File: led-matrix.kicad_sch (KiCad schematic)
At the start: 512 parts

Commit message: schematic updated
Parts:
- removed D129, D130, D131, D132, D133, D134, D135, D136, D137, D138, D139, D140, D141, D142, D143, D144, D145, D146, D147, D148, D149, D150, D151, D152, D153, D154, D155, D156, D157, D158, D159, D160, D161, D162, D163, D164, D165, D166, D167, D168, D169, D170, D171, D172, D173, D174, D175, D176, D177, D178, D179, D180, D181, D182, D183, D184, D185, D186, D187, D188, D189, D190, D191, D192, D193, D194, D195, D196, D197, D198, D199, D200, D201, D202, D203, D204, D205, D206, D207, D208, D209, D210, D211, D212, D213, D214, D215, D216, D217, D218, D219, D220, D221, D222, D223, D224, D225, D226, D227, D228, D229, D230, D231, D232, D233, D234, D235, D236, D237, D238, D239, D240, D241, D242, D243, D244, D245, D246, D247, D248, D249, D250, D251, D252, D253, D254, D255, D256, D257, D258, D259, D260, D261, D262, D263, D264, D265, D266, D267, D268, D269, D270, D271, D272, D273, D274, D275, D276, D277, D278, D279, D280, D281, D282, D283, D284, D285, D286, D287, D288, D289, D290, D291, D292, D293, D294, D295, D296, D297, D298, D299, D300, D301, D302, D303, D304, D305, D306, D307, D308, D309, D310, D311, D312, D313, D314, D315, D316, D317, D318, D319, D320, D321, D322, D323, D324, D325, D326, D327, D328, D329, D330, D331, D332, D333, D334, D335, D336, D337, D338, D339, D340, D341, D342, D343, D344, D345, D346, D347, D348, D349, D350, D351, D352, D353, D354, D355, D356, D357, D358, D359, D360, D361, D362, D363, D364, D365, D366, D367, D368, D369, D370, D371, D372, D373, D374, D375, D376, D377, D378, D379, D380, D381, D382, D383, D384, D385, D386, D387, D388, D389, D390, D391, D392, D393, D394, D395, D396, D397, D398, D399, D400, D401, D402, D403, D404, D405, D406, D407, D408, D409, D410, D411, D412, D413, D414, D415, D416, D417, D418, D419, D420, D421, D422, D423, D424, D425, D426, D427, D428, D429, D430, D431, D432, D433, D434, D435, D436, D437, D438, D439, D440, D441, D442, D443, D444, D445, D446, D447, D448, D449, D450, D451, D452, D453, D454, D455, D456, D457, D458, D459, D460, D461, D462, D463, D464, D465, D466, D467, D468, D469, D470, D471, D472, D473, D474, D475, D476, D477, D478, D479, D480, D481, D482, D483, D484, D485, D486, D487, D488, D489, D490, D491, D492, D493, D494, D495, D496, D497, D498, D499, D500, D501, D502, D503, D504, D505, D506, D507, D508, D509, D510, D511, D512: LED, PROJECT_FOOTPRINTS:LED_0805_2012Metric_45, symbol Device:LED
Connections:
- net at D118.1 (K), D22.1 (K), D54.1 (K)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: now also D102.1 (K), D38.1 (K), D6.1 (K), D70.1 (K)
- net at D81.2 (A), D82.2 (A), D83.2 (A)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: no longer D65.2 (A), D66.2 (A), D67.2 (A), D68.2 (A), D69.2 (A), D70.2 (A), D71.2 (A), D72.2 (A), D73.2 (A), D74.2 (A), D75.2 (A), D76.2 (A), D77.2 (A), D78.2 (A), D79.2 (A), D80.2 (A)
- net at D105.1 (K), D41.1 (K), D73.1 (K)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: now also D121.1 (K), D25.1 (K), D57.1 (K), D89.1 (K)
- net at D107.1 (K), D11.1 (K), D43.1 (K)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: now also D123.1 (K), D27.1 (K), D59.1 (K), D91.1 (K)
- net at D125.1 (K), D29.1 (K), D61.1 (K)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: now also D109.1 (K), D13.1 (K), D45.1 (K), D77.1 (K)
- net at D119.1 (K), D23.1 (K), D55.1 (K)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: now also D103.1 (K), D39.1 (K), D7.1 (K), D71.1 (K)
- net at D117.1 (K), D21.1 (K), D53.1 (K)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: now also D101.1 (K), D37.1 (K), D5.1 (K), D69.1 (K)
- net at D126.1 (K), D30.1 (K), D62.1 (K)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: now also D110.1 (K), D14.1 (K), D46.1 (K), D78.1 (K)
- net at D49.2 (A), D50.2 (A), D51.2 (A)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: no longer D33.2 (A), D34.2 (A), D35.2 (A), D36.2 (A), D37.2 (A), D38.2 (A), D39.2 (A), D40.2 (A), D41.2 (A), D42.2 (A), D43.2 (A), D44.2 (A), D45.2 (A), D46.2 (A), D47.2 (A), D48.2 (A)
- net at D122.1 (K), D26.1 (K), D58.1 (K)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: now also D10.1 (K), D106.1 (K), D42.1 (K), D74.1 (K)
- net at D120.1 (K), D24.1 (K), D56.1 (K)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: now also D104.1 (K), D40.1 (K), D72.1 (K), D8.1 (K)
- net at D114.1 (K), D18.1 (K), D50.1 (K)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: now also D2.1 (K), D34.1 (K), D66.1 (K), D98.1 (K)
- net at D115.1 (K), D19.1 (K), D51.1 (K)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: now also D3.1 (K), D35.1 (K), D67.1 (K), D99.1 (K)
- net at D128.1 (K), D32.1 (K), D64.1 (K)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: now also D112.1 (K), D16.1 (K), D48.1 (K), D80.1 (K)
- net at D100.1 (K), D36.1 (K), D4.1 (K)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: now also D116.1 (K), D20.1 (K), D52.1 (K), D84.1 (K)
- net at D111.1 (K), D15.1 (K), D47.1 (K)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: now also D127.1 (K), D31.1 (K), D63.1 (K), D95.1 (K)
- net at D17.2 (A), D18.2 (A), D19.2 (A)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: no longer D1.2 (A), D10.2 (A), D11.2 (A), D12.2 (A), D13.2 (A), D14.2 (A), D15.2 (A), D16.2 (A), D2.2 (A), D3.2 (A), D4.2 (A), D5.2 (A), D6.2 (A), D7.2 (A), D8.2 (A), D9.2 (A)
- net at D108.1 (K), D12.1 (K), D44.1 (K)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: now also D124.1 (K), D28.1 (K), D60.1 (K), D92.1 (K)
- net at D1.1 (K), D33.1 (K), D65.1 (K)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: now also D113.1 (K), D17.1 (K), D49.1 (K), D81.1 (K)
- net at D100.2 (A), D101.2 (A), D102.2 (A)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: no longer D113.2 (A), D114.2 (A), D115.2 (A), D116.2 (A), D117.2 (A), D118.2 (A), D119.2 (A), D120.2 (A), D121.2 (A), D122.2 (A), D123.2 (A), D124.2 (A), D125.2 (A), D126.2 (A), D127.2 (A), D128.2 (A)
- new net: D1.2 (A), D10.2 (A), D11.2 (A), D12.2 (A), D13.2 (A), D14.2 (A), D15.2 (A), D16.2 (A), D2.2 (A), D3.2 (A), D4.2 (A), D5.2 (A), D6.2 (A), D7.2 (A), D8.2 (A), D9.2 (A)
- new net: D113.2 (A), D114.2 (A), D115.2 (A), D116.2 (A), D117.2 (A), D118.2 (A), D119.2 (A), D120.2 (A), D121.2 (A), D122.2 (A), D123.2 (A), D124.2 (A), D125.2 (A), D126.2 (A), D127.2 (A), D128.2 (A)
- new net: D33.2 (A), D34.2 (A), D35.2 (A), D36.2 (A), D37.2 (A), D38.2 (A), D39.2 (A), D40.2 (A), D41.2 (A), D42.2 (A), D43.2 (A), D44.2 (A), D45.2 (A), D46.2 (A), D47.2 (A), D48.2 (A)
- new net: D65.2 (A), D66.2 (A), D67.2 (A), D68.2 (A), D69.2 (A), D70.2 (A), D71.2 (A), D72.2 (A), D73.2 (A), D74.2 (A), D75.2 (A), D76.2 (A), D77.2 (A), D78.2 (A), D79.2 (A), D80.2 (A)
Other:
- moved on the sheet: D1

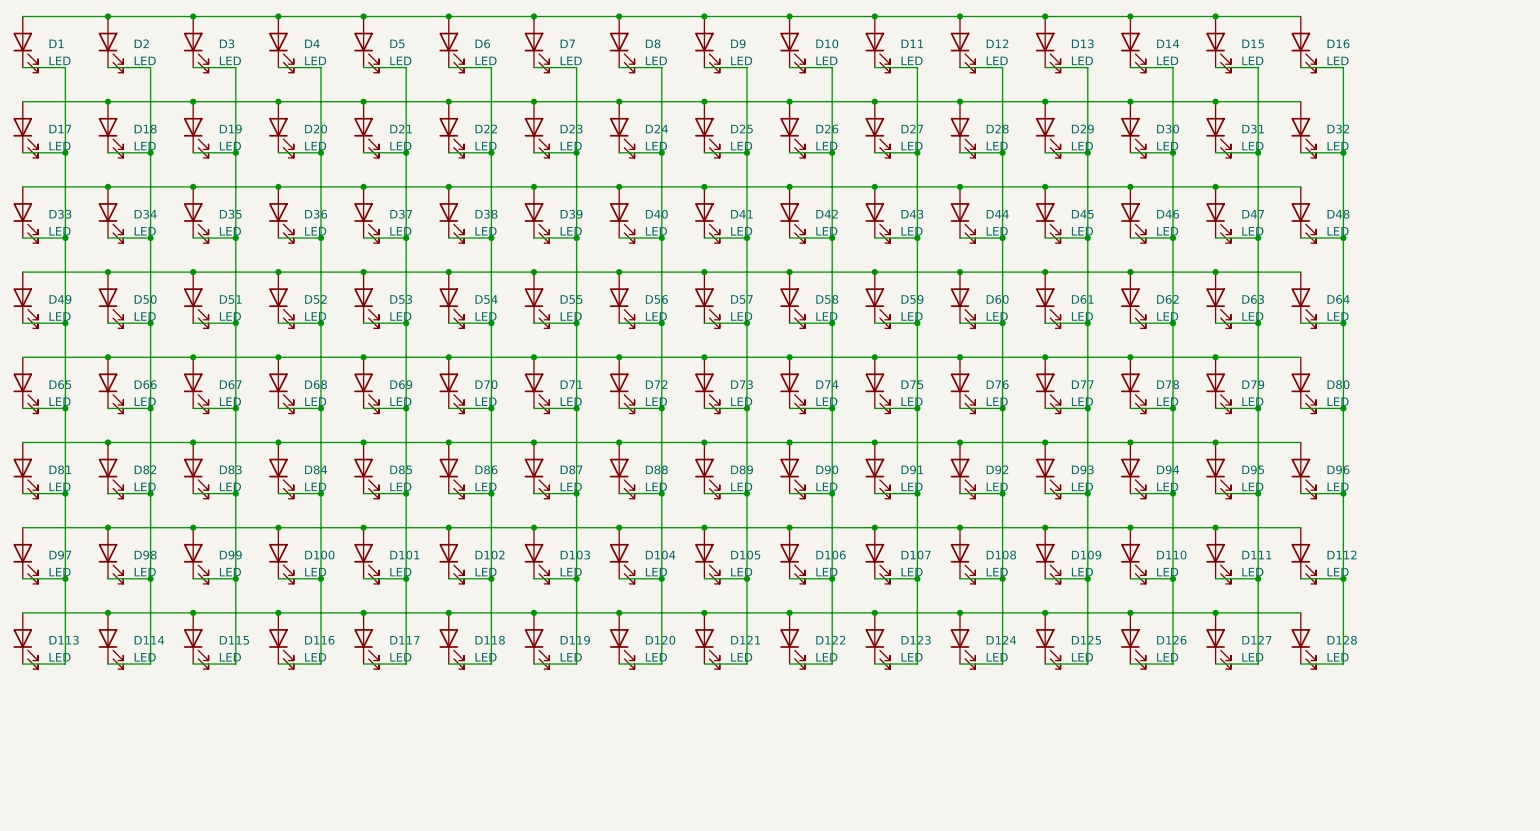
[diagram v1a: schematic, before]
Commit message: finished small design for testing, now sending to university pcb for fabrication
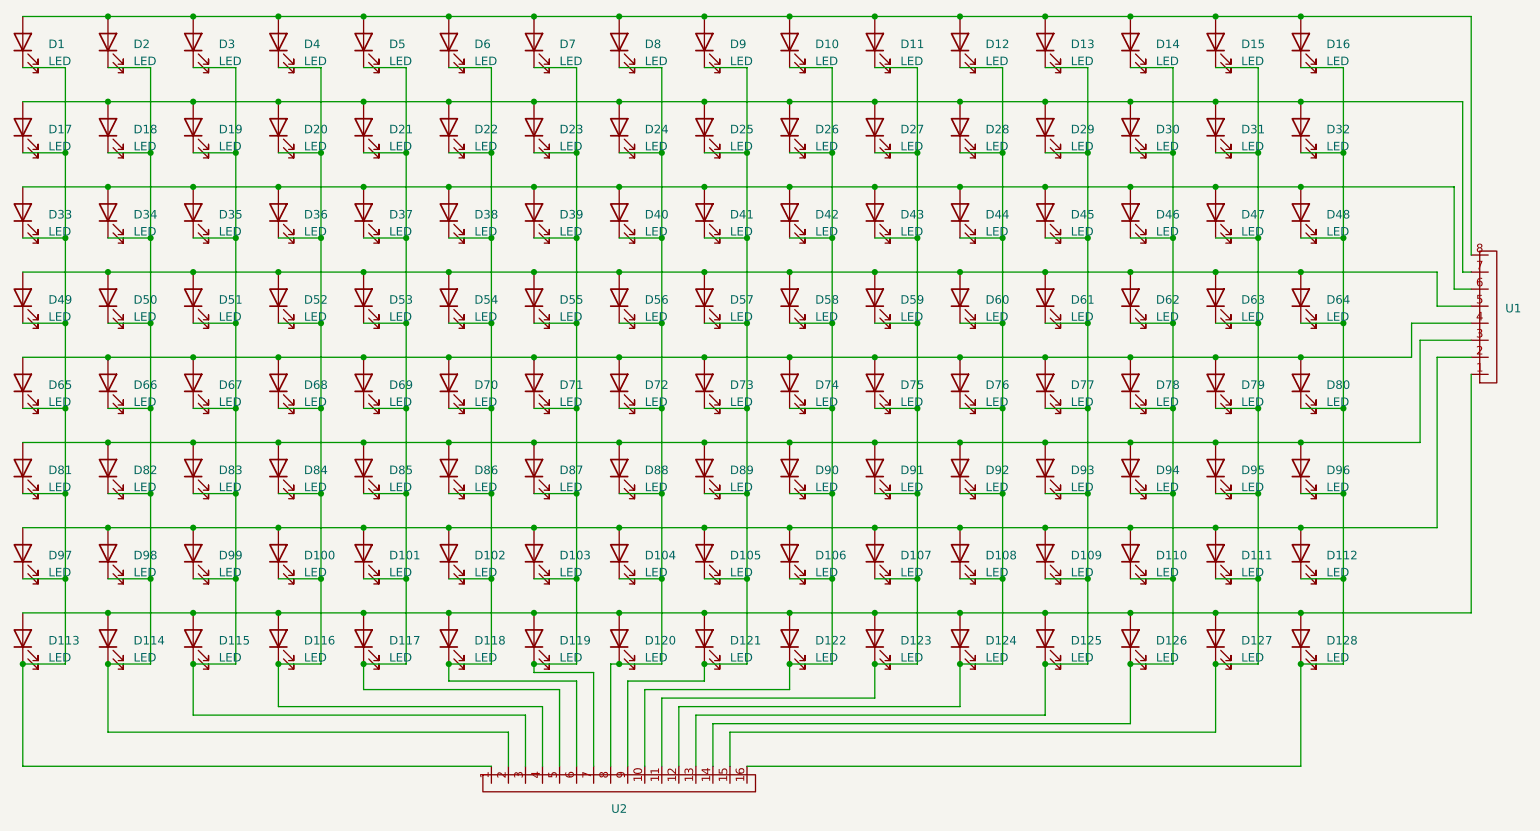
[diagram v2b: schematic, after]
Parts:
- added U1: ~, Connector_PinHeader_2.54mm:PinHeader_1x08_P2.54mm_Vertical, symbol PROJECT_SYMBOLS:CONNECTER8
- added U2: ~, Connector_PinHeader_2.54mm:PinHeader_1x16_P2.54mm_Vertical, symbol PROJECT_SYMBOLS:CONNECTOR16
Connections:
- net at D104.1 (K), D120.1 (K), D24.1 (K)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: now also U2.8
- net at D17.2 (A), D18.2 (A), D19.2 (A)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: now also U1.7
- net at D110.1 (K), D126.1 (K), D14.1 (K)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: now also U2.14
- net at D1.2 (A), D10.2 (A), D11.2 (A)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: now also U1.8
- net at D101.1 (K), D117.1 (K), D21.1 (K)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: now also U2.5
- net at D100.2 (A), D101.2 (A), D102.2 (A)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: now also U1.2
- net at D111.1 (K), D127.1 (K), D15.1 (K)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: now also U2.15
- net at D49.2 (A), D50.2 (A), D51.2 (A)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: now also U1.5
- net at D115.1 (K), D19.1 (K), D3.1 (K)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: now also U2.3
- net at D113.2 (A), D114.2 (A), D115.2 (A)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: now also U1.1
- net at D114.1 (K), D18.1 (K), D2.1 (K)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: now also U2.2
- net at D33.2 (A), D34.2 (A), D35.2 (A)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: now also U1.6
- net at D107.1 (K), D11.1 (K), D123.1 (K)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: now also U2.11
- net at D81.2 (A), D82.2 (A), D83.2 (A)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: now also U1.3
- net at D102.1 (K), D118.1 (K), D22.1 (K)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: now also U2.6
- net at D105.1 (K), D121.1 (K), D25.1 (K)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: now also U2.9
- net at D108.1 (K), D12.1 (K), D124.1 (K)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: now also U2.12
- net at D109.1 (K), D125.1 (K), D13.1 (K)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: now also U2.13
- net at D112.1 (K), D128.1 (K), D16.1 (K)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: now also U2.16
- net at D103.1 (K), D119.1 (K), D23.1 (K)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: now also U2.7
- net at D65.2 (A), D66.2 (A), D67.2 (A)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: now also U1.4
- net at D10.1 (K), D106.1 (K), D122.1 (K)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: now also U2.10
- net at D100.1 (K), D116.1 (K), D20.1 (K)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: now also U2.4
- net at D1.1 (K), D113.1 (K), D17.1 (K)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: now also U2.1

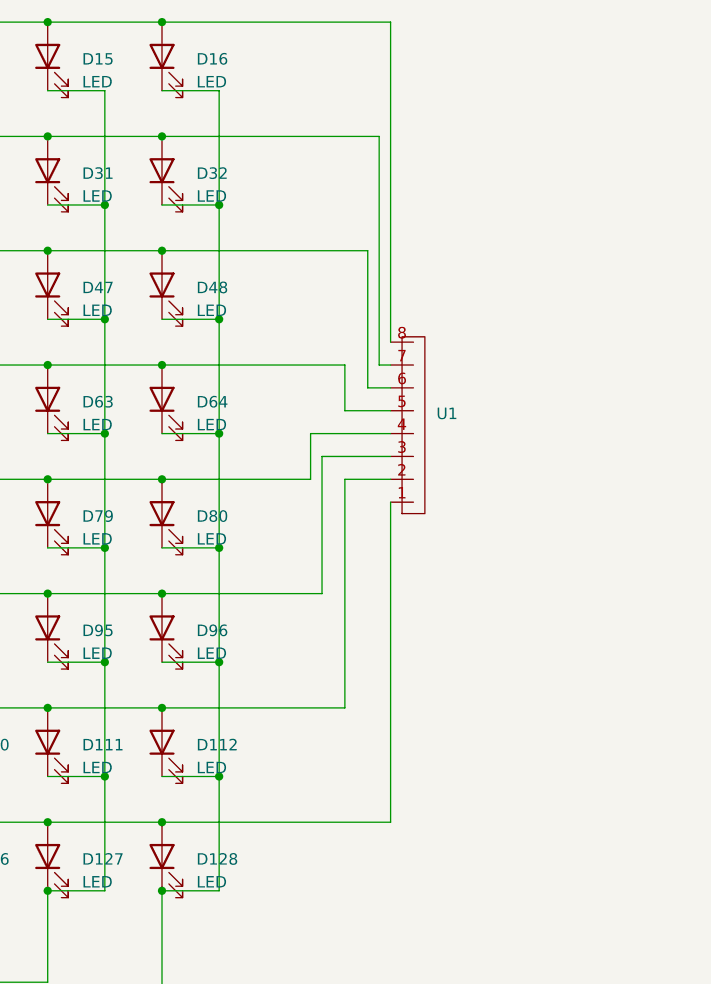
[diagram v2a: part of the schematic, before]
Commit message: added resistors to rows
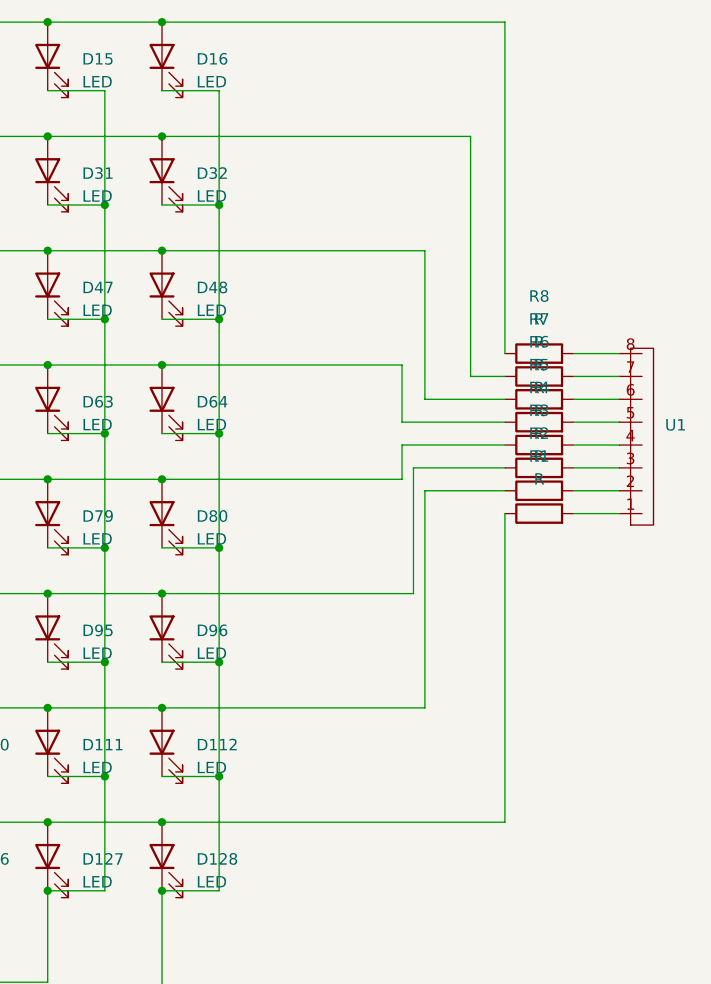
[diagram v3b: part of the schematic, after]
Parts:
- added R1, R2, R3, R4, R5, R6, R7, R8: R, Resistor_THT:R_Axial_DIN0207_L6.3mm_D2.5mm_P10.16mm_Horizontal, symbol Device:R
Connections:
- net at D17.2 (A), D18.2 (A), D19.2 (A)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: now also R7.1; no longer U1.7
- net at D1.2 (A), D10.2 (A), D11.2 (A)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: now also R8.1; no longer U1.8
- net at D100.2 (A), D101.2 (A), D102.2 (A)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: now also R2.1; no longer U1.2
- net at D49.2 (A), D50.2 (A), D51.2 (A)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: now also R5.1; no longer U1.5
- net at D113.2 (A), D114.2 (A), D115.2 (A)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: now also R1.1; no longer U1.1
- net at D33.2 (A), D34.2 (A), D35.2 (A)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: now also R6.1; no longer U1.6
- net at D81.2 (A), D82.2 (A), D83.2 (A)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: now also R3.1; no longer U1.3
- net at D65.2 (A), D66.2 (A), D67.2 (A)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: now also R4.1; no longer U1.4
- new net: R4.2, U1.4
- new net: R6.2, U1.6
- new net: R5.2, U1.5
- new net: R3.2, U1.3
- new net: R7.2, U1.7
- new net: R8.2, U1.8
- new net: R2.2, U1.2
- new net: R1.2, U1.1
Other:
- moved on the sheet: U1
